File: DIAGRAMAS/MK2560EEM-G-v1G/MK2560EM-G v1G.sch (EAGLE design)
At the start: 70 parts, among them U1 X-MOTOR, U2 Y-MOTOR, U3 Z-MOTOR

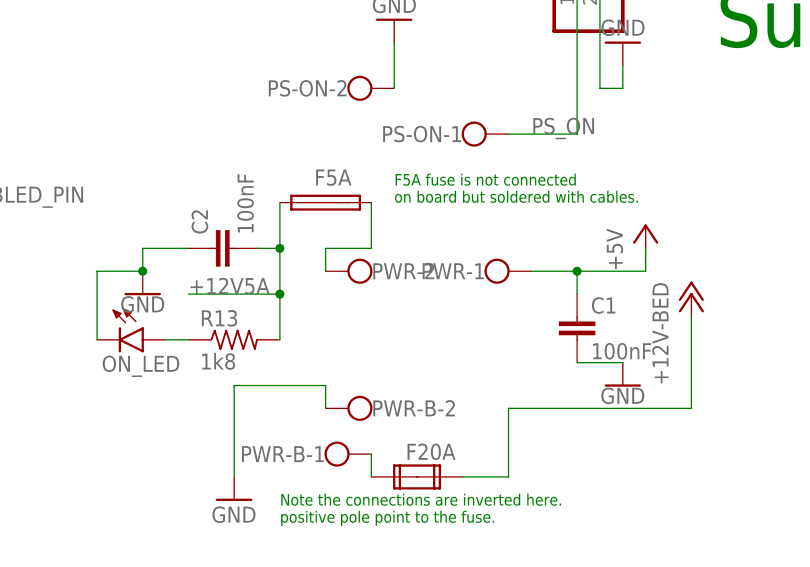
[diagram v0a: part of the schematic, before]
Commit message: new pcb optimizations
minor pcb error fixes and optimizations.
-changed some thermistors capacitors components for bigger ones.
- added silkscreen pdf for soldering reference.
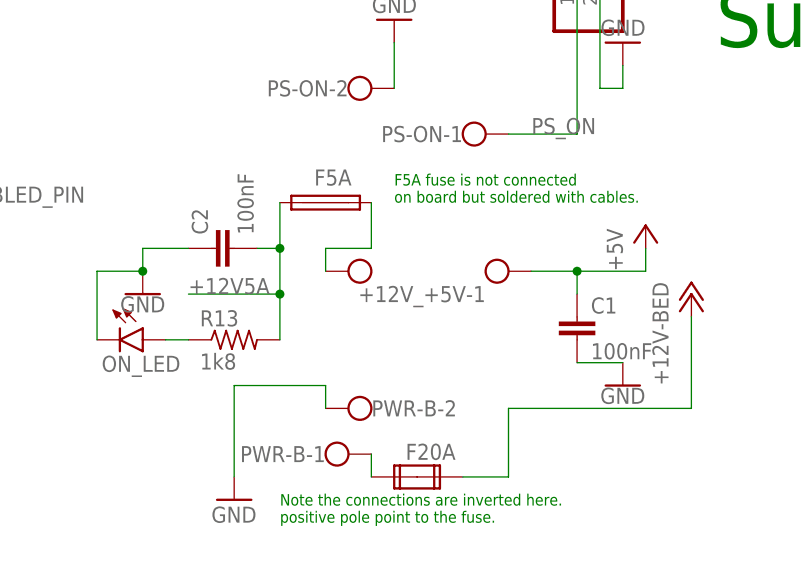
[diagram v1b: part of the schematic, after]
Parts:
- C3, C8: device rcl:CPOL-EUE2-4 -> rcl:CPOL-EUE2.5-6
- renumbered PWR to +12V_+5V
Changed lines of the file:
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@@
 <part name="EXT1" library="con-wago-500" library_urn="urn:adsk.eagle:library:195" deviceset="W237-102" device="" package3d_urn="urn:adsk.eagle:package:10688/1"/>
 <part name="R12" library="resistor" deviceset="R-US_" device="0204/7" value="4k7"/>
-<part name="C8" library="rcl" library_urn="urn:adsk.eagle:library:334" deviceset="CPOL-EU" device="E2-4" package3d_urn="urn:adsk.eagle:package:23347/1" value="10uf"/>
+<part name="C8" library="rcl" library_urn="urn:adsk.eagle:library:334" deviceset="CPOL-EU" device="E2.5-6" package3d_urn="urn:adsk.eagle:package:23349/1" value="10uf"/>
 <part name="GND12" library="SparkFun-PowerSymbols" deviceset="GND" device=""/>
 <part name="P+15" library="supply1" library_urn="urn:adsk.eagle:library:371" deviceset="+5V" device=""/>
@@
 <part name="GND14" library="SparkFun-PowerSymbols" deviceset="GND" device=""/>
 <part name="R9" library="resistor" deviceset="R-US_" device="0204/7" value="4k7"/>
-<part name="C3" library="rcl" library_urn="urn:adsk.eagle:library:334" deviceset="CPOL-EU" device="E2-4" package3d_urn="urn:adsk.eagle:package:23347/1" value="10uf"/>
+<part name="C3" library="rcl" library_urn="urn:adsk.eagle:library:334" deviceset="CPOL-EU" device="E2.5-6" package3d_urn="urn:adsk.eagle:package:23349/1" value="10uf"/>
 <part name="GND6" library="SparkFun-PowerSymbols" deviceset="GND" device=""/>
 <part name="P+6" library="supply1" library_urn="urn:adsk.eagle:library:371" deviceset="+5V" device=""/>
@@
 <part name="FAN2" library="pinhead" library_urn="urn:adsk.eagle:library:325" deviceset="PINHD-1X2" device="" package3d_urn="urn:adsk.eagle:package:22435/2"/>
 <part name="PS-ON" library="con-wago-500" library_urn="urn:adsk.eagle:library:195" deviceset="W237-102" device="" package3d_urn="urn:adsk.eagle:package:10688/1"/>
-<part name="PWR" library="con-wago-500" library_urn="urn:adsk.eagle:library:195" deviceset="W237-102" device="" package3d_urn="urn:adsk.eagle:package:10688/1"/>
+<part name="+12V_+5V" library="con-wago-500" library_urn="urn:adsk.eagle:library:195" deviceset="W237-102" device="" package3d_urn="urn:adsk.eagle:package:10688/1"/>
 <part name="PWR-B" library="con-wago-500" library_urn="urn:adsk.eagle:library:195" deviceset="W237-102" device="" package3d_urn="urn:adsk.eagle:package:10688/1"/>
 <part name="GND23" library="supply1" library_urn="urn:adsk.eagle:library:371" deviceset="GND" device=""/>
@@
 <attribute name="NAME" x="-241.3" y="282.829" size="1.778" layer="95" rot="R180"/>
 </instance>
-<instance part="PWR" gate="-1" x="-226.06" y="261.62" smashed="yes">
-<attribute name="NAME" x="-226.06" y="262.509" size="1.778" layer="95" rot="R180"/>
-</instance>
-<instance part="PWR" gate="-2" x="-238.76" y="261.62" smashed="yes" rot="R180">
+<instance part="+12V_+5V" gate="-1" x="-226.06" y="261.62" smashed="yes">
+<attribute name="NAME" x="-226.06" y="259.969" size="1.778" layer="95" rot="R180"/>
+</instance>
+<instance part="+12V_+5V" gate="-2" x="-238.76" y="261.62" smashed="yes" rot="R180">
 <attribute name="VALUE" x="-236.22" y="265.303" size="1.778" layer="96" rot="R180"/>
-<attribute name="NAME" x="-238.76" y="260.731" size="1.778" layer="95"/>
 </instance>
 <instance part="PWR-B" gate="-1" x="-243.84" y="241.3" smashed="yes">
@@
 <pinref part="C1" gate="G$1" pin="1"/>
 <wire x1="-215.9" y1="261.62" x2="-215.9" y2="259.08" width="0.1524" layer="91"/>
-<pinref part="PWR" gate="-1" pin="KL"/>
+<pinref part="+12V_+5V" gate="-1" pin="KL"/>
 <wire x1="-215.9" y1="261.62" x2="-220.98" y2="261.62" width="0.1524" layer="91"/>
 <junction x="-215.9" y="261.62"/>
@@
 <wire x1="-238.76" y1="269.24" x2="-238.76" y2="264.16" width="0.1524" layer="91"/>
 <wire x1="-238.76" y1="264.16" x2="-243.84" y2="264.16" width="0.1524" layer="91"/>
-<pinref part="PWR" gate="-2" pin="KL"/>
+<pinref part="+12V_+5V" gate="-2" pin="KL"/>
 <wire x1="-243.84" y1="264.16" x2="-243.84" y2="261.62" width="0.1524" layer="91"/>
 </segment>
